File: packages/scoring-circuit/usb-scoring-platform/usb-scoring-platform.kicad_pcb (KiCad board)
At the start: 4 copper layers, 160 x 100 mm, 155 parts, among them J1 GCT USB4105-GF-A, J10 5520250-2, J2 STM SWD 3.3V, J3 LEFT WEAPON A B C, J4 RIGHT WEAPON A B C, J5 PISTE - NOT protective earth, J6 ESP 3.3V UART recovery, J7 TST-108-02-G-D - HUB75, J8 645004114822 - panel 5V, J9 5520250-2, Q1 BSS138-7-F, Q2 BSS138-7-F, Q3 BSS138-7-F, SW1 STM RESET, SW2 ESP RESET, SW3 ESP BOOT, U1 STM32G474RET6, U10 SN74AXC1T45DCKR, U11 SN74AXC1T45DCKR, U12 WIZ850io, U13 TSOP38438, U14 SN74AHCT245PWR, U15 SN74AHCT245PWR, U16 4N32M, U17 4N32M, U18 LTM2884IY#PBF, U2 ESP32-S3-WROOM-1-N8R8, U3 TPD2E2U06DCKR, U4 AP2112K-3.3TRG1, U5 Adafruit 5807 - set 20V, U6 D36V50F5, U7 AP63203WU-7, U8 74LVC125APW, U9 74LVC125APW, Y1 ABM3B-8.000MHZ-B2-T

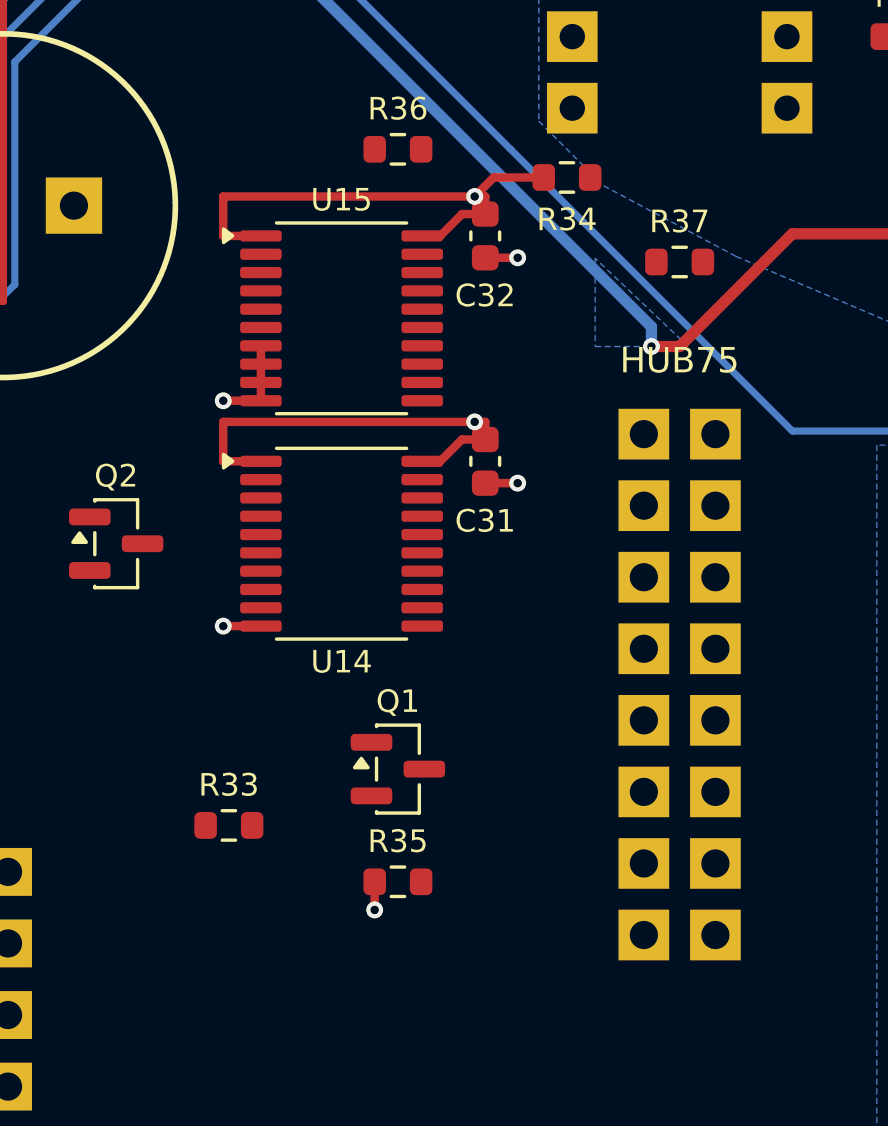
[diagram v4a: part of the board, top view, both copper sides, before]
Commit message: feat(scoring-circuit): route HUB75 outputs and blanking network
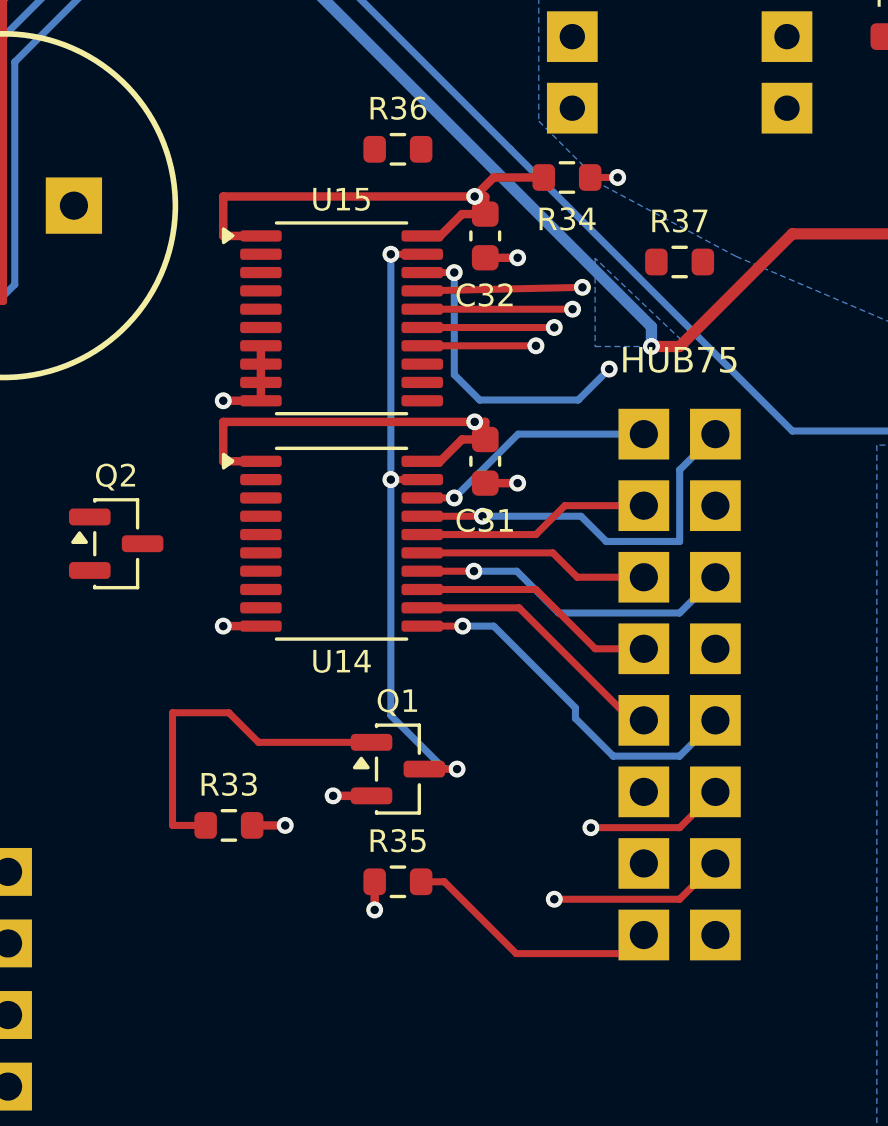
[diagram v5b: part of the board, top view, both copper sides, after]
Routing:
- net PANEL_OE: track 0.00 -> 38.0 mm, vias 0 -> 1
- net RGB_BUFFER_OE_N: track 0.00 -> 33.1 mm, vias 0 -> 4
- net PANEL_LAT: track 0.00 -> 31.2 mm, vias 0 -> 2
- net PANEL_D: track 0.00 -> 29.9 mm, vias 0 -> 2
- net PANEL_CLK: track 0.00 -> 27.5 mm, vias 0 -> 1
- net PANEL_C: track 0.00 -> 27.3 mm, vias 0 -> 2
- net PANEL_G1: track 0.00 -> 13.8 mm, vias 0 -> 1
- net PANEL_B: track 0.00 -> 13.1 mm, vias 0 -> 1
- net DISPLAY_ENABLE: track 0.00 -> 12.7 mm
- net PANEL_G2: track 0.00 -> 11.5 mm, vias 0 -> 1
- net PANEL_A: track 0.00 -> 9.52 mm
- net PANEL_R1: track 0.00 -> 8.81 mm, vias 0 -> 1
- net PANEL_B2: track 0.00 -> 8.74 mm
- net PANEL_B1: track 0.00 -> 8.29 mm
- net PANEL_R2: track 0.00 -> 8.23 mm
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
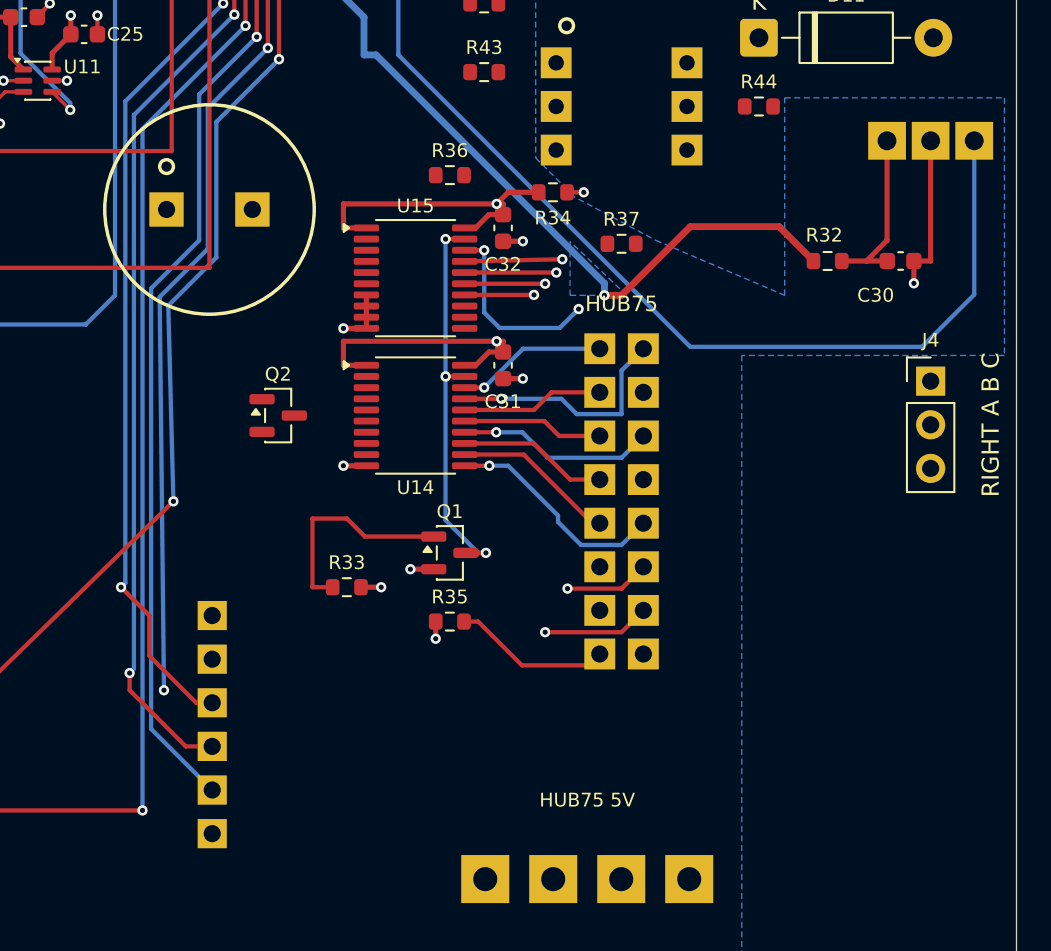
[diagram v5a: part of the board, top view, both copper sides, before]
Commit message: fix(scoring-circuit): define HUB75 buffer reset states
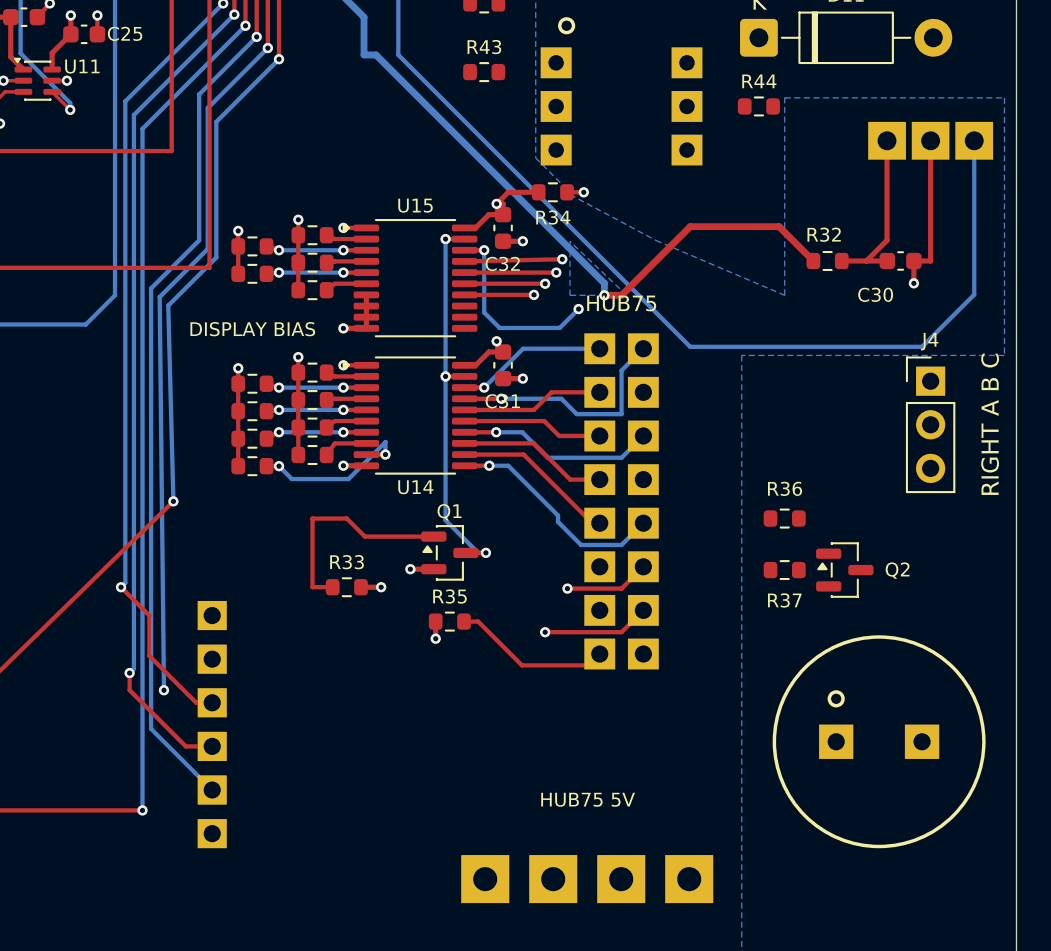
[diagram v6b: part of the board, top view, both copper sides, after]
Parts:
- added R74: 10k 1%, Resistor_SMD:R_0603_1608Metric, F.Cu at (169.0, 114.5)
- added R75: 10k 1%, Resistor_SMD:R_0603_1608Metric, F.Cu at (165.5, 115.2)
- added R76: 10k 1%, Resistor_SMD:R_0603_1608Metric, F.Cu at (169.0, 116.1)
- added R77: 10k 1%, Resistor_SMD:R_0603_1608Metric, F.Cu at (165.5, 116.8)
- added R78: 10k 1%, Resistor_SMD:R_0603_1608Metric, F.Cu at (169.0, 117.7)
- added R79: 10k 1%, Resistor_SMD:R_0603_1608Metric, F.Cu at (165.5, 118.3)
- added R80: 10k 1%, Resistor_SMD:R_0603_1608Metric, F.Cu at (169.0, 119.3)
- added R81: 10k 1%, Resistor_SMD:R_0603_1608Metric, F.Cu at (165.5, 120.0)
- added R82: 10k 1%, Resistor_SMD:R_0603_1608Metric, F.Cu at (169.0, 106.5)
- added R83: 10k 1%, Resistor_SMD:R_0603_1608Metric, F.Cu at (165.5, 107.2)
- added R84: 10k 1%, Resistor_SMD:R_0603_1608Metric, F.Cu at (169.0, 108.1)
- added R85: 10k 1%, Resistor_SMD:R_0603_1608Metric, F.Cu at (165.5, 108.8)
- added R86: 10k 1%, Resistor_SMD:R_0603_1608Metric, F.Cu at (169.0, 109.7)
- U14, U15: value SN74AHCT245PWR -> SN74AHCT541PWR
- moved BZ1 49.8 mm to (202.0, 136.0)
- moved Q2 34.2 mm to (200.0, 126.0)
- moved R36 27.9 mm to (196.5, 123.0)
- moved R37 21.2 mm to (196.5, 126.0)
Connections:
- U14 pad 1: PANEL_5V -> GND
- U15 pad 1: PANEL_5V -> GND
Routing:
- net PANEL_5V: track 109.9 -> 85.5 mm
- net GND: track 97.8 -> 118.5 mm, vias 63 -> 69
- net RGB_B: track 0.00 -> 9.96 mm, vias 0 -> 2
- net RGB_B2: track 0.00 -> 5.90 mm, vias 0 -> 2
- net RGB_G1: track 0.00 -> 5.85 mm, vias 0 -> 2
- net RGB_D: track 0.00 -> 5.85 mm, vias 0 -> 2
- net RGB_R2: track 0.00 -> 5.82 mm, vias 0 -> 2
- net RGB_LAT: track 0.00 -> 5.82 mm, vias 0 -> 2
- net RGB_A: track 0.00 -> 2.66 mm
- net RGB_OE: track 0.00 -> 2.44 mm
- net RGB_G2: track 0.00 -> 2.44 mm
- net RGB_R1: track 0.00 -> 2.36 mm
- net RGB_C: track 0.00 -> 2.36 mm
- net RGB_CLK: track 0.00 -> 2.32 mm
- net RGB_B1: track 0.00 -> 2.32 mm
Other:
- board text added: "DISPLAY BIAS"

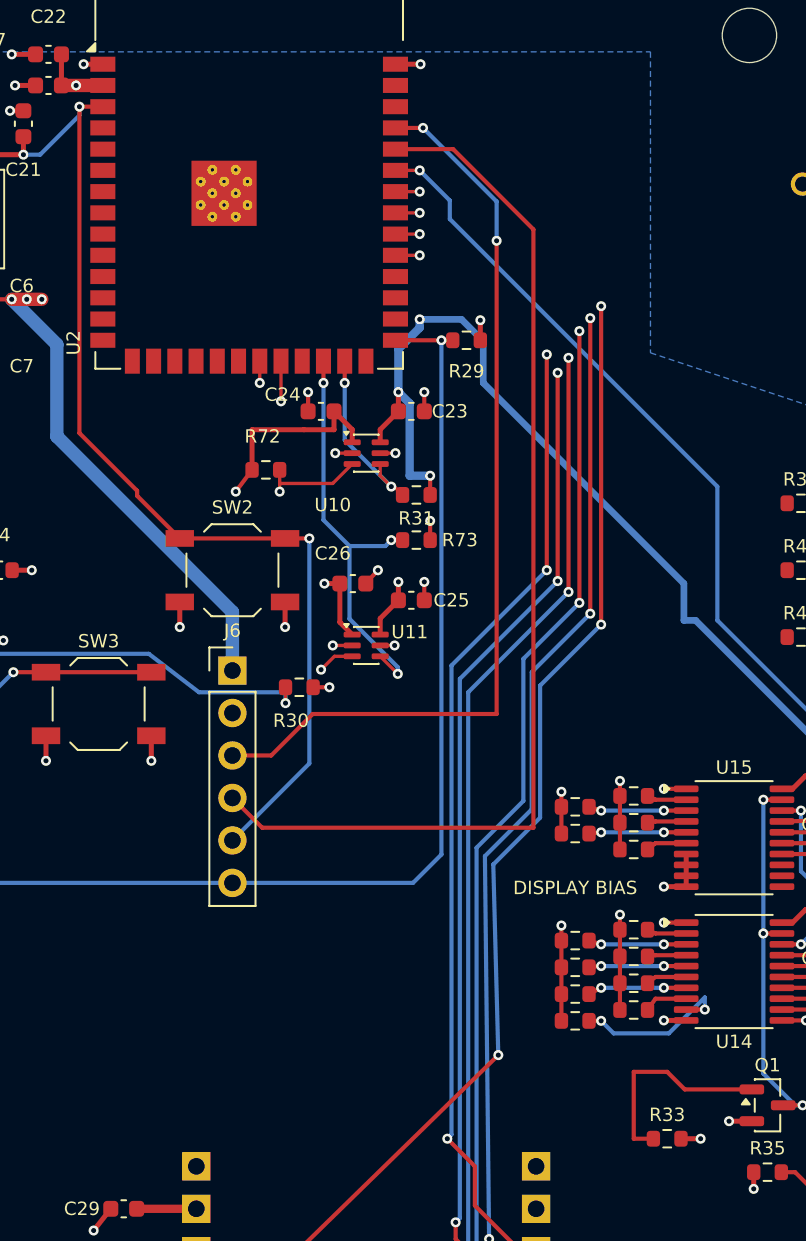
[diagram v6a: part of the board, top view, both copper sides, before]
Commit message: feat(scoring-circuit): route ESP32 HUB75 input bus
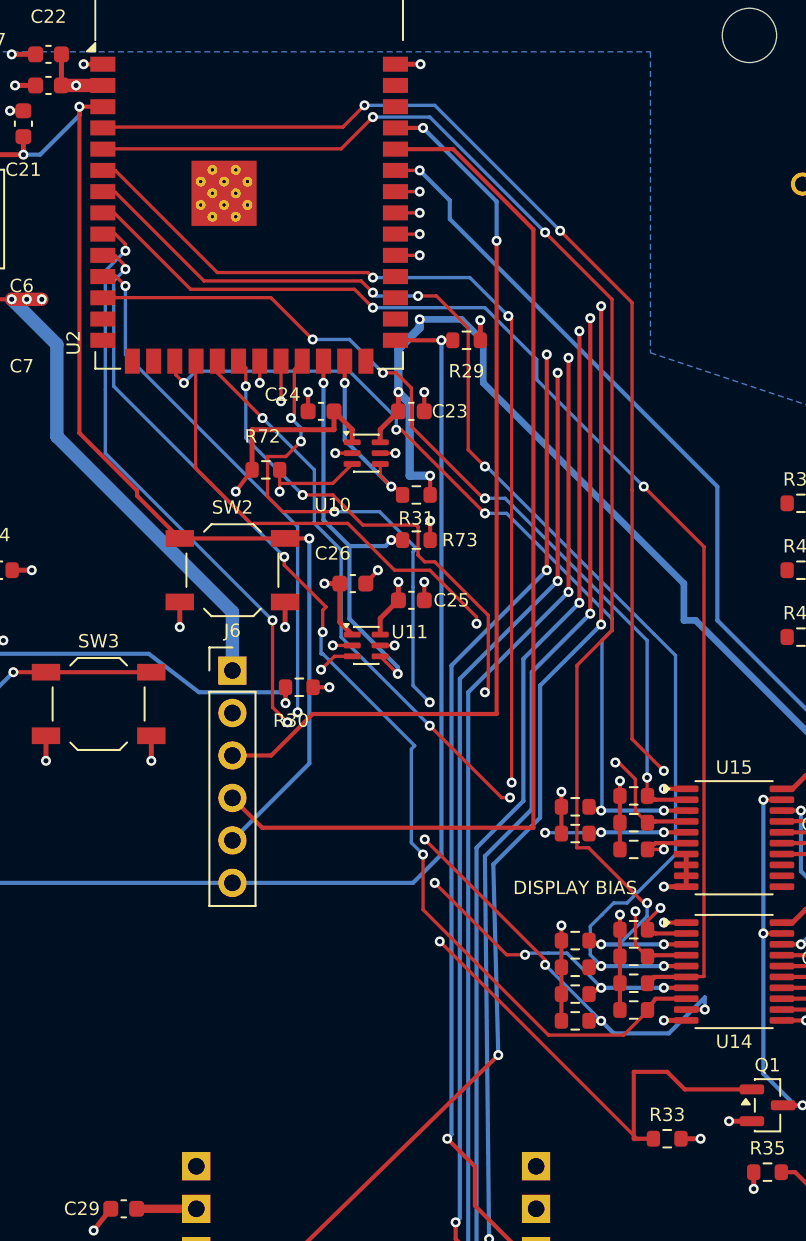
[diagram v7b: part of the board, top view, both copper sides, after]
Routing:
- net RGB_G1: track 5.85 -> 85.2 mm, vias 2 -> 5
- net RGB_R1: track 2.36 -> 78.9 mm, vias 0 -> 4
- net RGB_G2: track 2.44 -> 76.8 mm, vias 0 -> 2
- net RGB_R2: track 5.82 -> 77.5 mm, vias 2 -> 5
- net RGB_B1: track 2.32 -> 72.0 mm, vias 0 -> 4
- net RGB_A: track 2.66 -> 68.5 mm, vias 0 -> 4
- net DISPLAY_ENABLE: track 12.7 -> 75.3 mm, vias 0 -> 5
- net RGB_B2: track 5.90 -> 67.2 mm, vias 2 -> 7
- net RGB_B: track 9.96 -> 67.6 mm, vias 2 -> 6
- net RGB_C: track 2.36 -> 54.2 mm, vias 0 -> 4
- net RGB_D: track 5.85 -> 51.6 mm, vias 2 -> 5
- net RGB_OE: track 2.44 -> 47.4 mm, vias 0 -> 4
- net RGB_CLK: track 2.32 -> 46.0 mm, vias 0 -> 2
- net RGB_LAT: track 5.82 -> 45.9 mm, vias 2 -> 6

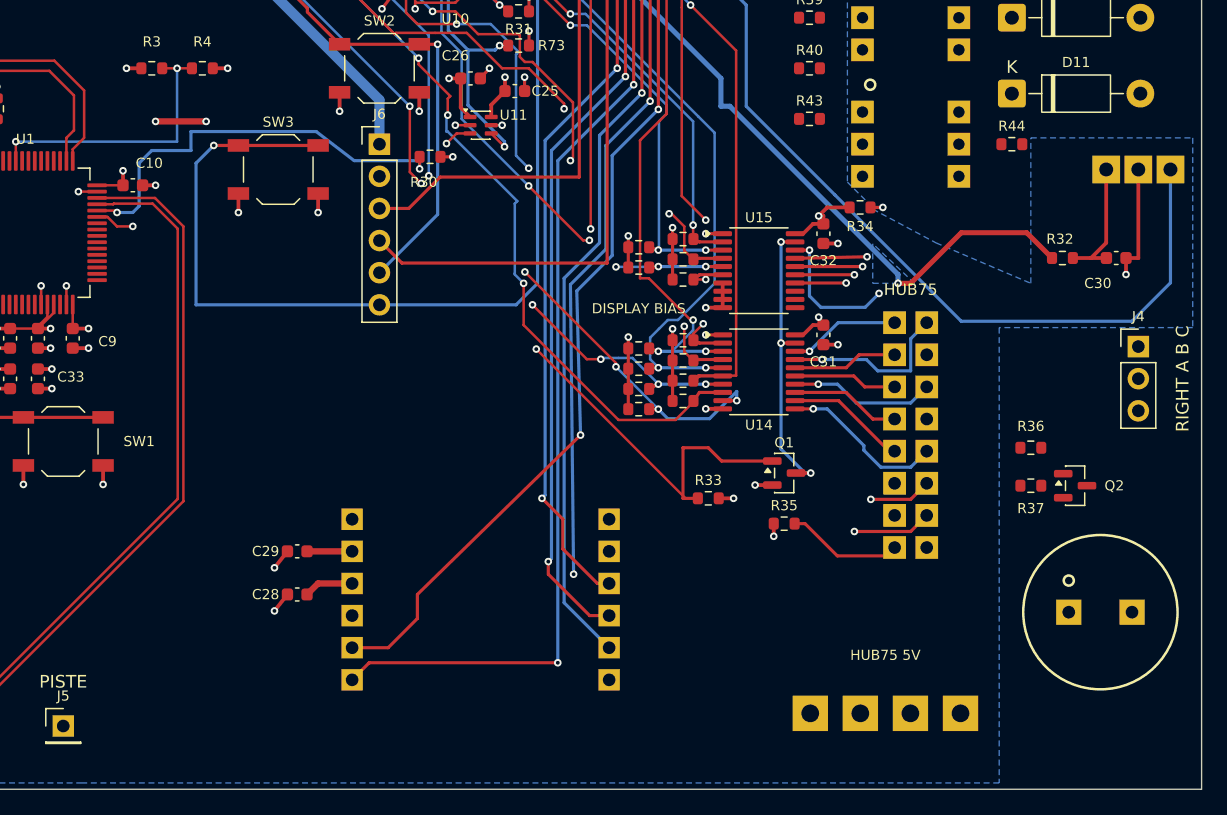
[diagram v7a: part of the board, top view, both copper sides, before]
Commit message: fix(scoring-circuit): complete piezo sounder drive and routing
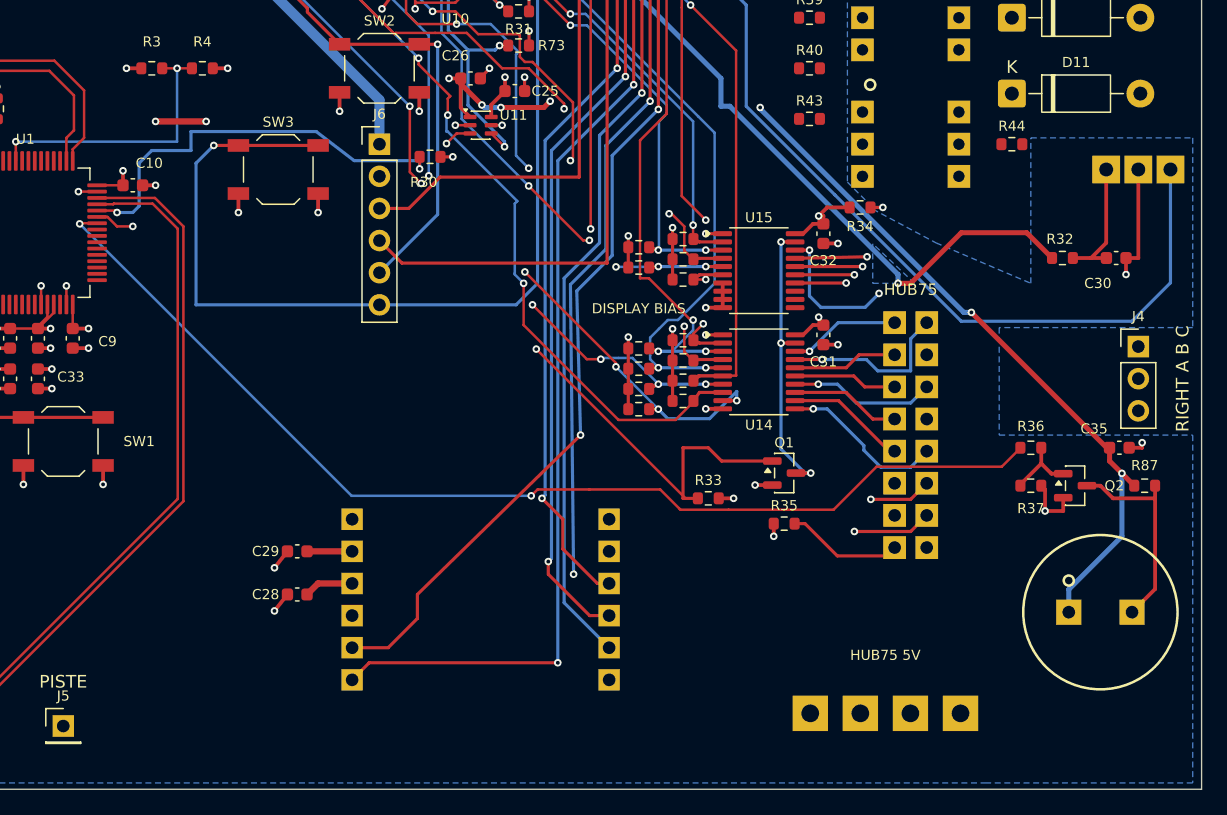
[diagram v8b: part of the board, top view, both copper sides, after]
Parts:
- added C35: 100nF, Capacitor_SMD:C_0603_1608Metric, F.Cu at (203.5, 123.0)
- added R87: 1k 1%, Resistor_SMD:R_0603_1608Metric, F.Cu at (205.5, 126.0)
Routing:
- net SOUNDER_PWM: track 0.00 -> 87.9 mm, vias 0 -> 2
- net CORE_3V3: track 86.3 -> 168.0 mm, vias 18 -> 24
- net BUZZER_LOW: track 0.00 -> 16.6 mm
- net GND: track 118.5 -> 124.5 mm, vias 69 -> 71
- net BUZZER_GATE: track 0.00 -> 5.75 mm
